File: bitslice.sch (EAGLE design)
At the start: 22 parts

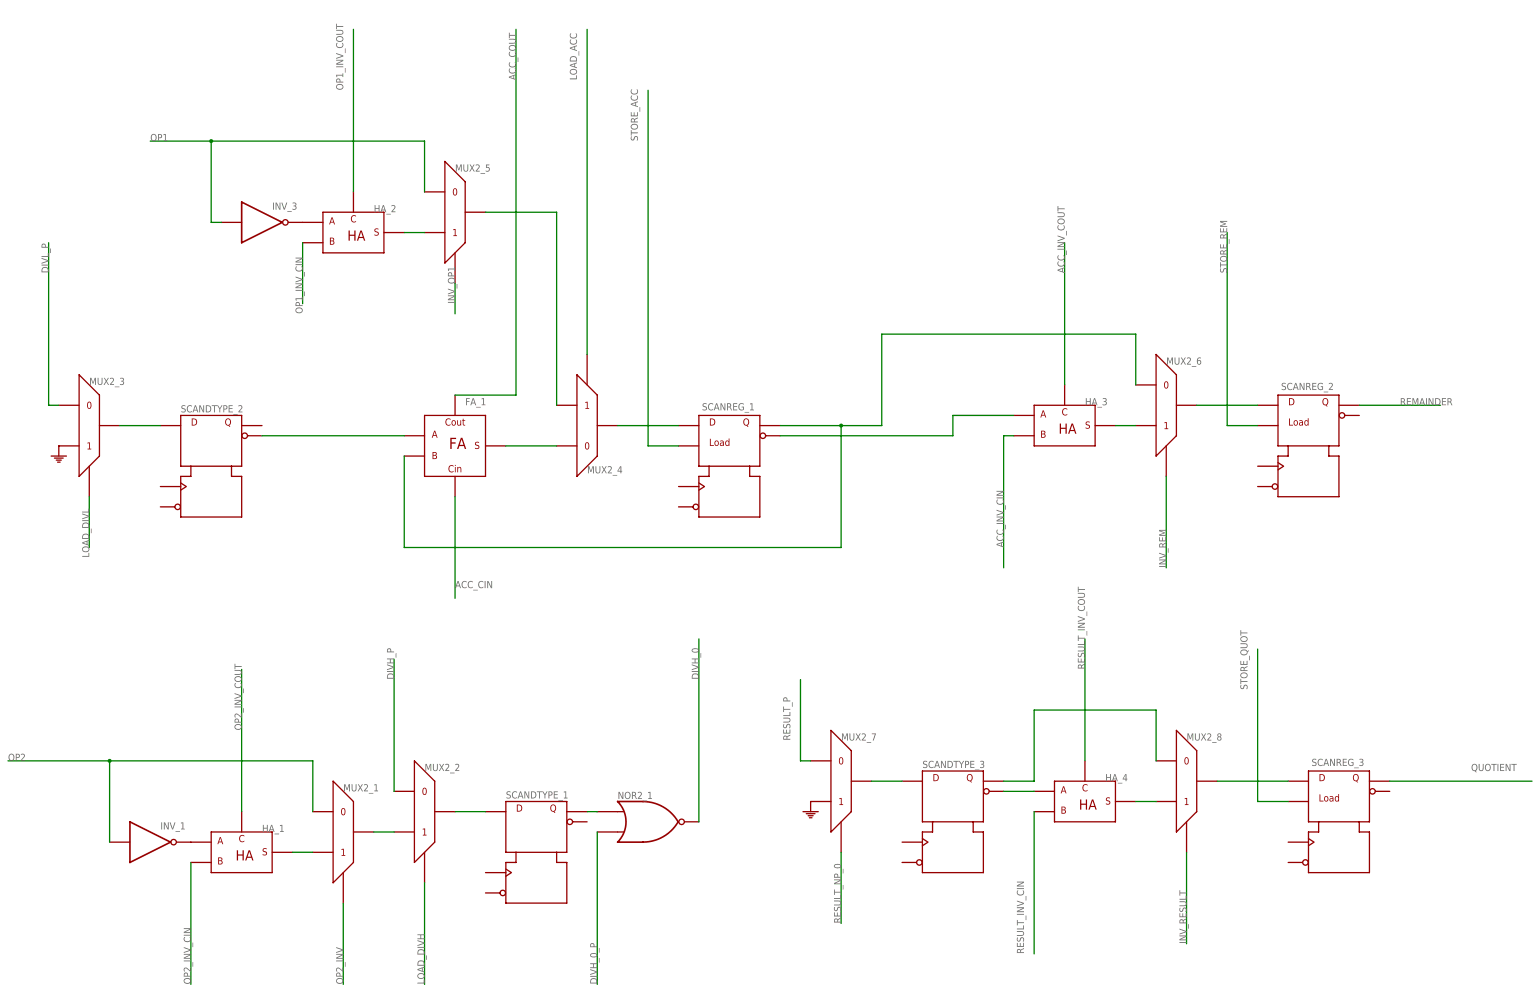
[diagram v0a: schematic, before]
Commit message: Checked against magic design. Named parts with same numbers as magic design. All port names are consistent. ish
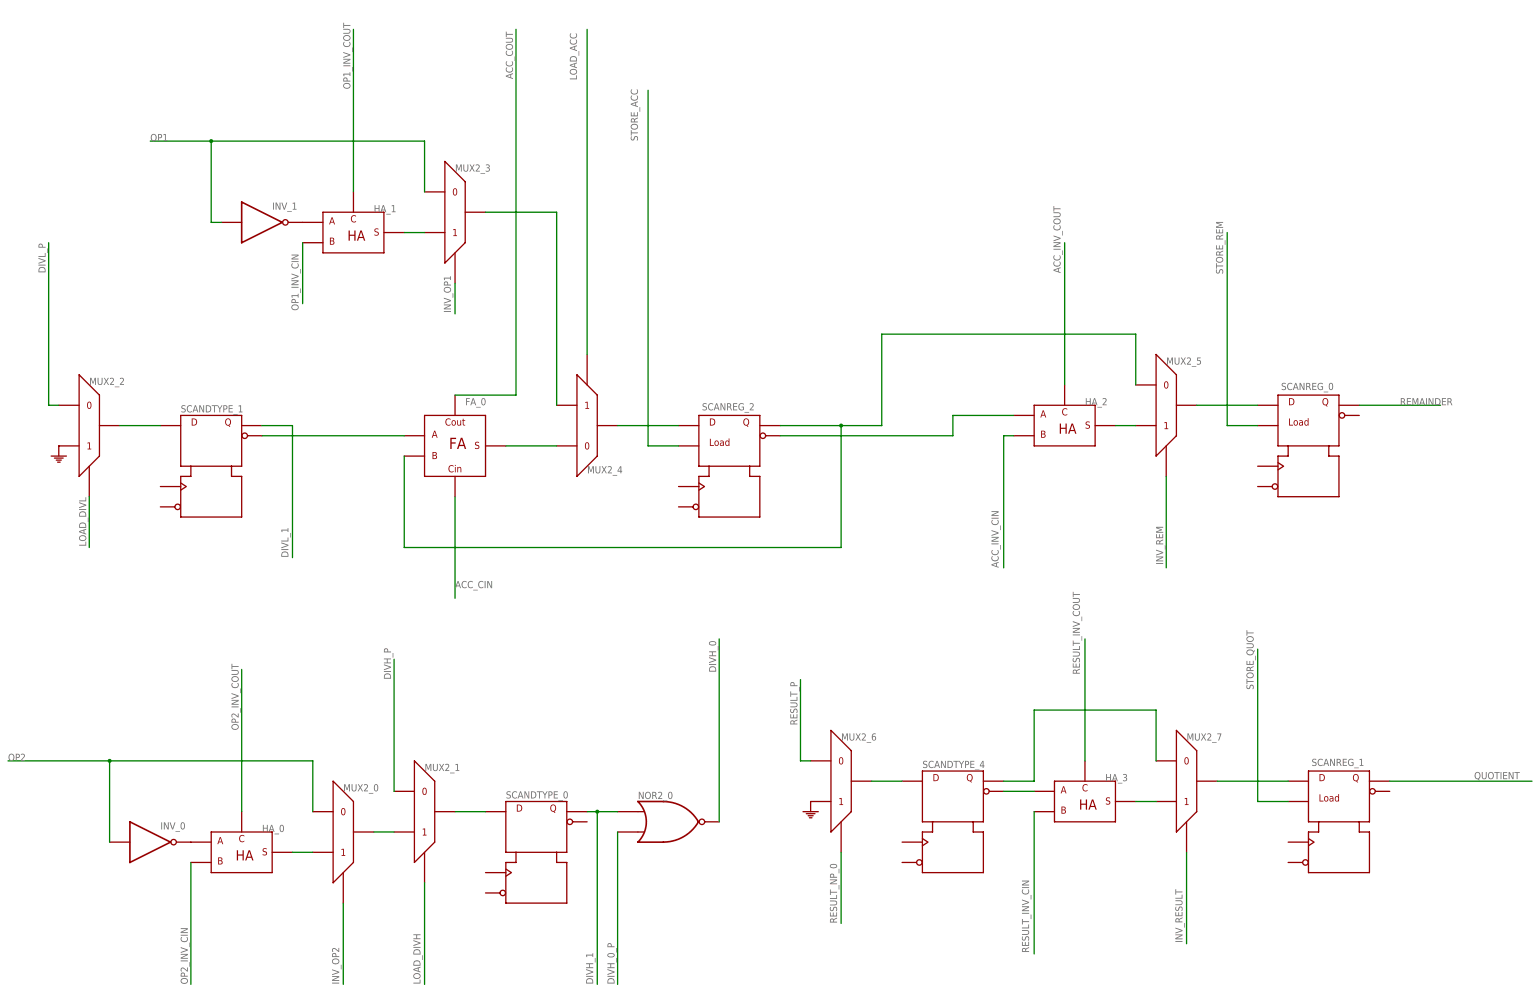
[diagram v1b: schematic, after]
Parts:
- removed HA_4: HALFADDER, c035u:HALFADDER
- removed INV_3: INV, c035u:INV
- removed MUX2_8: MUX2, c035u:MUX2
- removed NOR2_1: NOR2, c035u:NOR2
- removed SCANDTYPE_2: SCANDTYPE, c035u:SCANDTYPE
- removed SCANREG_3: SCANREG, c035u:SCANREG
- added HA_0: HALFADDER, c035u:HALFADDER
- added INV_0: INV, c035u:INV
- added MUX2_0: MUX2, c035u:MUX2
- added NOR2_0: NOR2, c035u:NOR2
- added SCANDTYPE_0: SCANDTYPE, c035u:SCANDTYPE
- added SCANREG_0: SCANREG, c035u:SCANREG
- renumbered FA_1 to FA_0, SCANDTYPE_3 to SCANDTYPE_4
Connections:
- removed net N$10 (its old number): HA_3.S, MUX2_6.P$2
- removed net N$12 (its old number): HA_2.A, INV_3.O
- removed net N$4: NOR2_1.I0, SCANDTYPE_1.Q
- removed net N$7 (its old number): MUX2_3.P$3, SCANDTYPE_2.D
- removed net OP2_INV: MUX2_1.P$4
- new net DIVH_1: NOR2_0.I0, SCANDTYPE_0.Q
- new net DIVL_1: SCANDTYPE_1.Q
- new net INV_OP2: MUX2_0.P$4
- new net N$1: HA_0.A, INV_0.O
- new net N$13: HA_1.S, MUX2_3.P$2
- new net N$2: MUX2_1.P$3, SCANDTYPE_0.D
- net ACC_INV_CIN: now also HA_2.B; no longer HA_3.B
- net ACC_INV_COUT: now also HA_2.COUT; no longer HA_3.COUT
- net DIVH_0: now also NOR2_0.O; no longer NOR2_1.O
- net DIVH_0_P: now also NOR2_0.I1; no longer NOR2_1.I1
- net DIVH_P: now also MUX2_1.P$1; no longer MUX2_2.P$1
- net DIVL_P: now also MUX2_2.P$1; no longer MUX2_3.P$1
- net INV_OP1: now also MUX2_3.P$4; no longer MUX2_5.P$4
- net INV_REM: now also MUX2_5.P$4; no longer MUX2_6.P$4
- net INV_RESULT: now also MUX2_7.P$4; no longer MUX2_8.P$4
- net LOAD_DIVH: now also MUX2_1.P$4; no longer MUX2_2.P$4
- net LOAD_DIVL: now also MUX2_2.P$4; no longer MUX2_3.P$4
- net N$14: now also HA_3.A; no longer HA_4.A
- net N$15: now also HA_3.S, MUX2_7.P$2; no longer HA_4.S, MUX2_8.P$2
- net N$16: now also MUX2_7.P$1; no longer MUX2_8.P$1
- net N$17: now also MUX2_7.P$3, SCANREG_1.D; no longer MUX2_8.P$3, SCANREG_3.D
- net N$19: now also MUX2_3.P$3; no longer MUX2_5.P$3
- net N$22: now also SCANREG_2.D; no longer SCANREG_1.D
- net N$23: now also MUX2_5.P$1, SCANREG_2.Q; no longer MUX2_6.P$1, SCANREG_1.Q
- net N$25: now also MUX2_5.P$3, SCANREG_0.D; no longer MUX2_6.P$3, SCANREG_2.D
- net N$3: now also HA_0.S, MUX2_0.P$2; no longer HA_1.S, MUX2_1.P$2
- net N$5: now also MUX2_6.P$3; no longer MUX2_7.P$3
- net N$6: now also MUX2_0.P$3, MUX2_1.P$2; no longer MUX2_1.P$3, MUX2_2.P$2
- net N$8: now also HA_2.A, SCANREG_2.NQ; no longer HA_3.A, SCANREG_1.NQ
- net N$9: now also SCANDTYPE_1.NQ; no longer SCANDTYPE_2.NQ
- net OP1: now also INV_1.I, MUX2_3.P$1; no longer INV_3.I, MUX2_5.P$1
- net OP1_INV_CIN: now also HA_1.B; no longer HA_2.B
- net OP1_INV_COUT: now also HA_1.COUT; no longer HA_2.COUT
- net OP2: now also INV_0.I, MUX2_0.P$1; no longer INV_1.I, MUX2_1.P$1
- net OP2_INV_CIN: now also HA_0.B; no longer HA_1.B
- net OP2_INV_COUT: now also HA_0.COUT; no longer HA_1.COUT
- net PE: now also MUX2_2.P$2, MUX2_6.P$2; no longer MUX2_3.P$2, MUX2_7.P$2
- net QUOTIENT: now also SCANREG_1.Q; no longer SCANREG_3.Q
- net REMAINDER: now also SCANREG_0.Q; no longer SCANREG_2.Q
- net RESULT_INV_CIN: now also HA_3.B; no longer HA_4.B
- net RESULT_INV_COUT: now also HA_3.COUT; no longer HA_4.COUT
- net RESULT_NP_0: now also MUX2_6.P$4; no longer MUX2_7.P$4
- net RESULT_P: now also MUX2_6.P$1; no longer MUX2_7.P$1
- net STORE_ACC: now also SCANREG_2.LOAD; no longer SCANREG_1.LOAD
- net STORE_QUOT: now also SCANREG_1.LOAD; no longer SCANREG_3.LOAD
- net STORE_REM: now also SCANREG_0.LOAD; no longer SCANREG_2.LOAD
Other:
- moved on the sheet: HA_1, HA_2, HA_3, INV_1, MUX2_1, MUX2_2, MUX2_3, MUX2_5, MUX2_6, MUX2_7, SCANDTYPE_1, SCANREG_1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

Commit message: Added Clock and nReset signals to the schematic
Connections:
- new net CLOCK: SCANDTYPE_0.CLOCK, SCANDTYPE_1.CLOCK, SCANDTYPE_4.CLOCK, SCANREG_0.CLOCK, SCANREG_1.CLOCK, SCANREG_2.CLOCK
- new net NRESET: SCANDTYPE_0.NRESET, SCANDTYPE_1.NRESET, SCANDTYPE_4.NRESET, SCANREG_1.NRESET, SCANREG_2.NRESET
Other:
- moved on the sheet: HA_1, HA_2, HA_3, INV_1, MUX2_3, MUX2_5, MUX2_6, MUX2_7, SCANDTYPE_4, SCANREG_0, SCANREG_1

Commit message: Added labels for internal signals Match the magic design
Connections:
- net N$10 renamed HA_2_S
- net N$13 renamed HA_1_S
- net N$16 renamed RESULT_1
- net N$19 renamed MUX2_3_Y
- net N$20 renamed FA_0_S
- net N$22 renamed ACC_D
- net N$23 renamed ACC_Q
- net N$25 renamed REM_D
- net N$7 renamed MUX2_2_Y
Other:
- note added: "Accumulator"
- note added: "DIVH"
- note added: "DIVL"
- note added: "Quotient"
- note added: "RESULT"
- note added: "Remainder"
